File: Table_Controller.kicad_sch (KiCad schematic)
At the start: 173 parts, among them J10 1050171001 Micro Type B, J11 HX JN1.27-2x5 WZ H4.9, J12 Conn_01x04_Pin, J13 Conn_01x14_Pin, J14 2.54 mm header, J15 2.54 mm header, U10 STM32G431K8Tx, U11 LMR380x0, U12 VNH7070, Y10 20 MHz

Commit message: placement 95%
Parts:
- removed JP31: 0R, Resistor_THT:R_Axial_DIN0204_L3.6mm_D1.6mm_P5.08mm_Horizontal, symbol Device:R
- removed JP35: 0R, Personal:Jumper_0603, symbol Device:R
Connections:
- net S19V5: now also C25.1, C27.1, U12.12 (VCC), U12.4 (VCC), U12.5 (VCC)
- net S3V3: now also J14.4 (Pin_4)

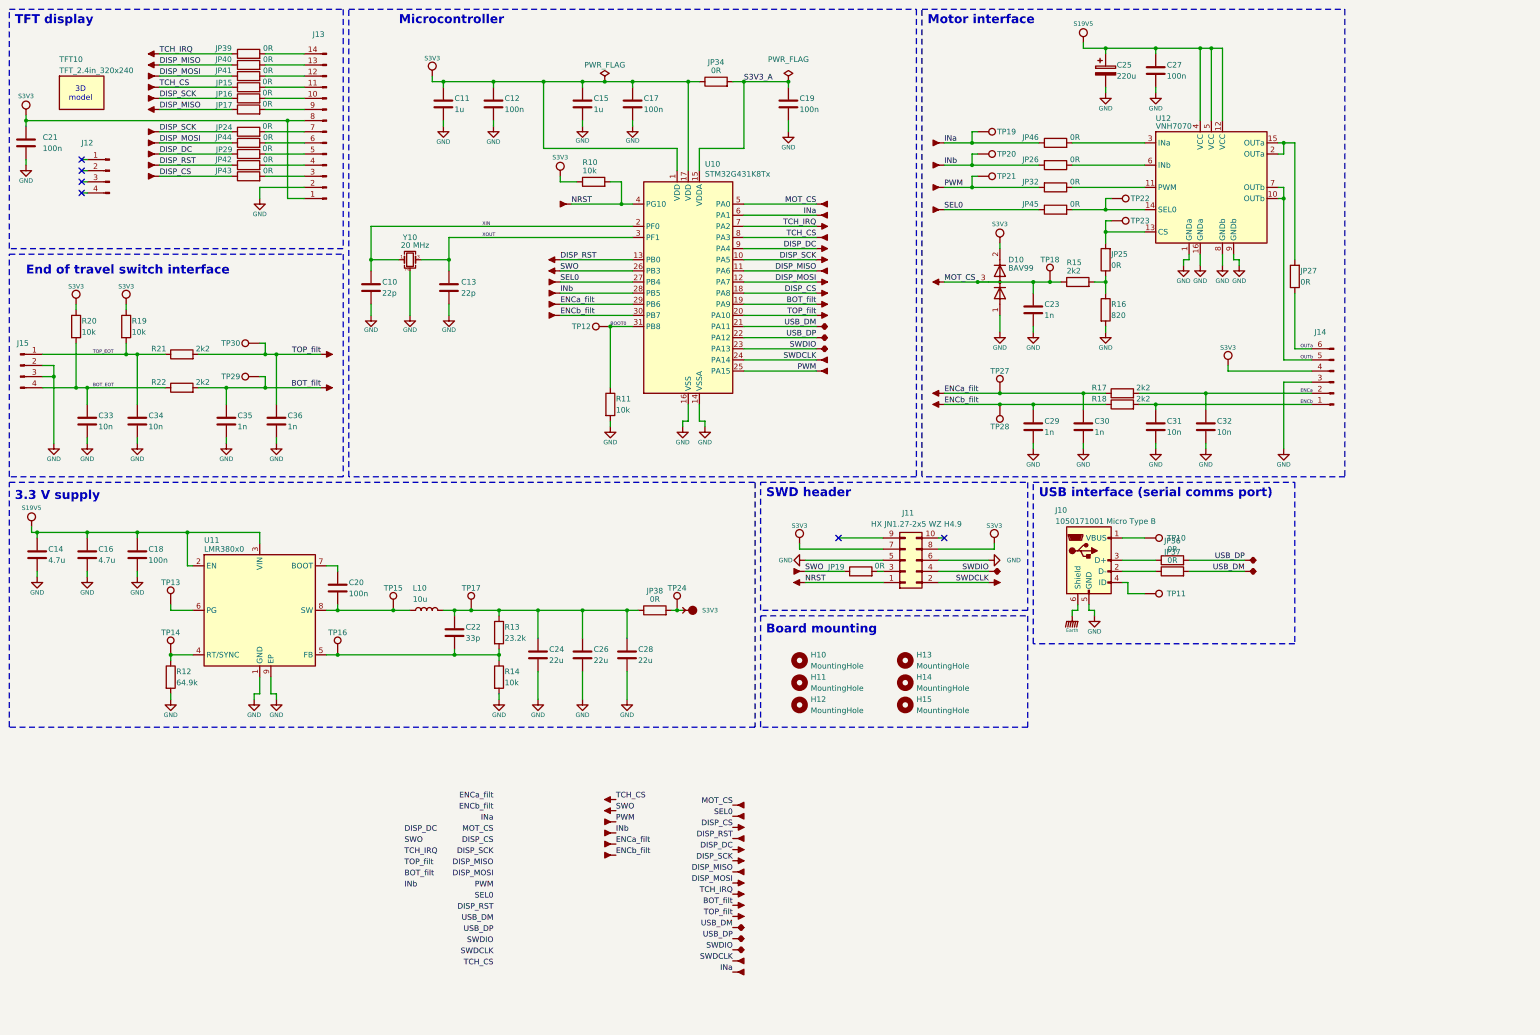
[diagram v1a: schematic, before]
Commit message: new usb connector
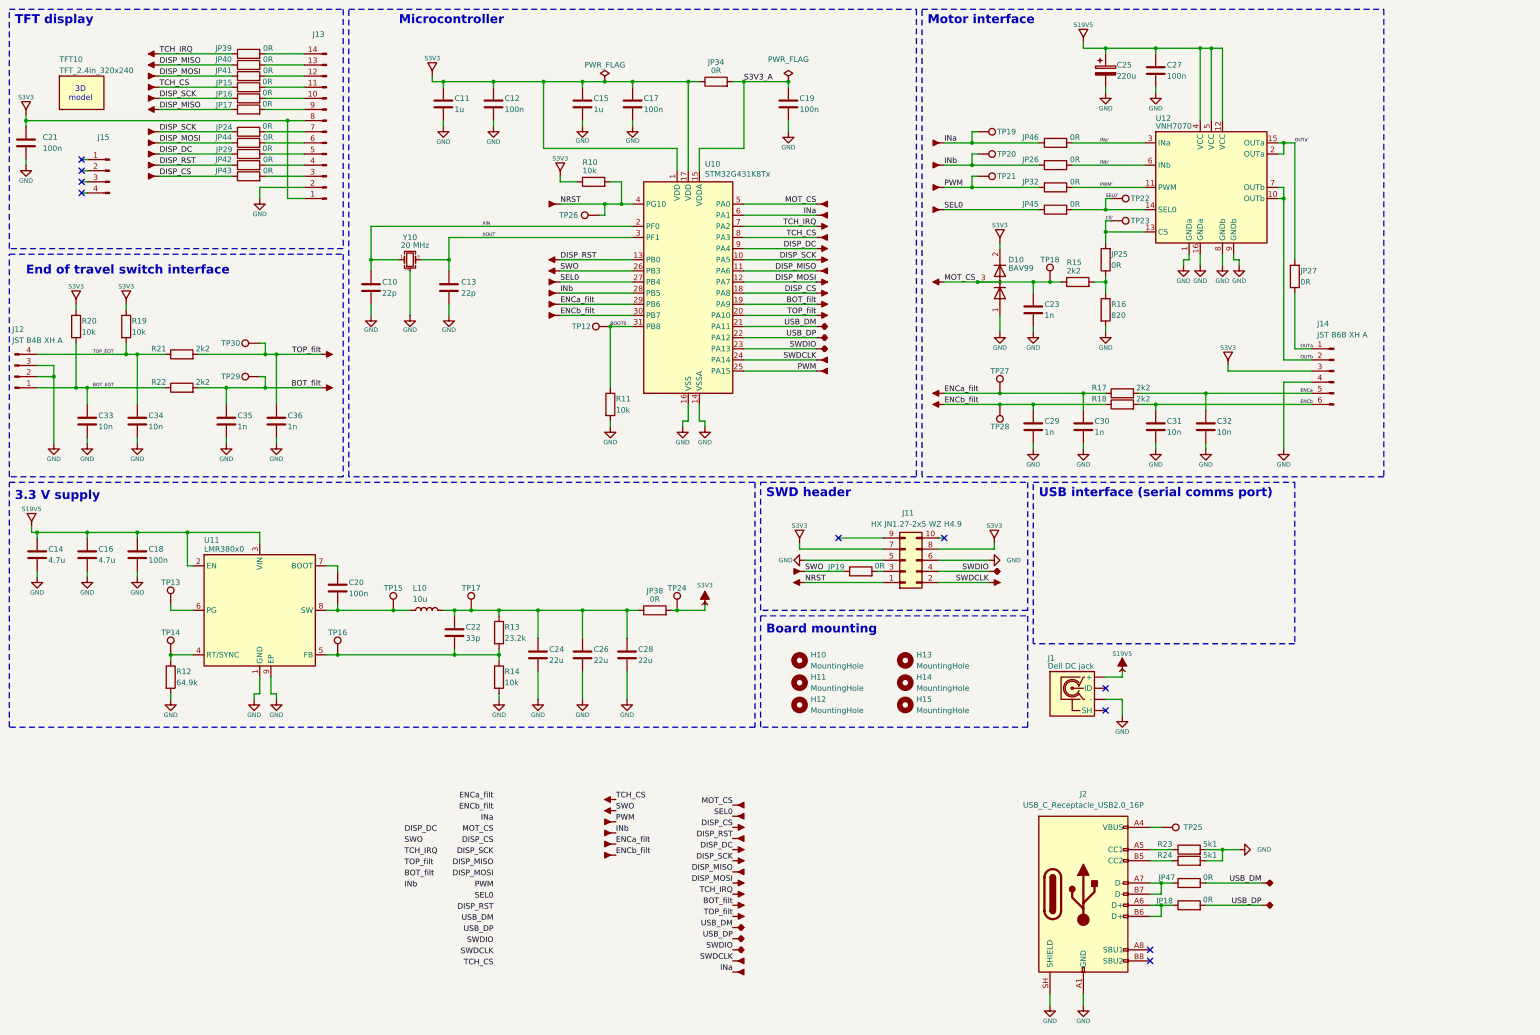
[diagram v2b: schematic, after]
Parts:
- removed J10: 1050171001 Micro Type B, Personal:USB_Micro-B_Molex-105017-0001, symbol Connector:USB_B_Micro
- removed JP36, JP37: 0R, Personal:Jumper_0603, symbol Device:R
- removed P14, P15: (no value), symbol personal:Cosmetic_IO
- removed TP10, TP11: TestPoint, TestPoint:TestPoint_THTPad_D1.0mm_Drill0.5mm, symbol Connector:TestPoint
- added J1: Dell DC jack, Personal:Dell DC jack, symbol personal:Dell_DC_barrel_jack
- added J2: USB_C_Receptacle_USB2.0_16P, Personal:USB_C_socket_16P_vertical, symbol Connector:USB_C_Receptacle_USB2.0_16P
- added JP18: 0R, Resistor_SMD:R_0603_1608Metric_Pad0.98x0.95mm_HandSolder, symbol Device:R
- added JP47: 0R, Personal:Jumper_0603, symbol Device:R
- added P81, P82: (no value), symbol personal:Cosmetic_IO
- added R23, R24: 5k1, Resistor_SMD:R_0603_1608Metric_Pad0.98x0.95mm_HandSolder, symbol Device:R
- added TP25, TP26: TestPoint, TestPoint:TestPoint_THTPad_D1.0mm_Drill0.5mm, symbol Connector:TestPoint
- J11: footprint Personal:HX JN1.27-2x5P ZZ H4.9 -> Personal:JN1.27-2x5 WZ H4.9
- J12: value Conn_01x04_Pin -> JST B4B XH A; footprint Connector_PinSocket_2.54mm:PinSocket_1x04_P2.54mm_Vertical -> Connector_JST:JST_XH_B4B-XH-A_1x04_P2.50mm_Vertical
- J14: value 2.54 mm header -> JST B6B XH A; footprint Connector_PinHeader_2.54mm:PinHeader_1x06_P2.54mm_Vertical -> Connector_JST:JST_XH_B6B-XH-A_1x06_P2.50mm_Vertical
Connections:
- net BOT_EOT: now also J12.1 (Pin_1); no longer J15.4 (Pin_4)
- net ENCa: now also J14.5 (Pin_5); no longer J14.2 (Pin_2)
- net ENCb: now also J14.6 (Pin_6); no longer J14.1 (Pin_1)
- net GND: now also J12.2 (Pin_2), J12.3 (Pin_3), J14.4 (Pin_4), J1.3 (-), J2.A1 (GND), J2.A12 (GND), J2.B1 (GND), J2.B12 (GND), J2.SH (SHIELD), R23.2, R24.2; no longer J14.3 (Pin_3), J15.2 (Pin_2), J15.3 (Pin_3)
- net NRST: now also TP26.1
- net OUTa: now also J14.1 (Pin_1); no longer J14.6 (Pin_6)
- net OUTb: now also J14.2 (Pin_2); no longer J14.5 (Pin_5)
- net S19V5: now also J1.1 (+)
- net S3V3: now also J14.3 (Pin_3); no longer J14.4 (Pin_4)
- net TOP_EOT: now also J12.4 (Pin_4); no longer J15.1 (Pin_1)
- net USB_DM: now also JP47.2, P82.1
- net USB_DP: now also JP18.2, P81.1
- net SEL0': now reaches JP45.2, TP22.1, U12.14 (SEL0)
- net CS': now reaches JP25.2, TP23.1, U12.13 (CS)
- net INa': now reaches JP46.2, U12.3 (INa)
- net PWM': now reaches JP32.1, U12.11 (PWM)
- net OUTa': now reaches JP27.2, U12.15 (OUTa), U12.2 (OUTa)
- net INb': now reaches JP26.1, U12.6 (INb)
- new net: J2.A5 (CC1), R23.1
- new net: J2.A4 (VBUS), J2.A9 (VBUS), J2.B4 (VBUS), J2.B9 (VBUS), TP25.1
- new net: J2.A6 (D+), J2.B6 (D+), JP18.1
- new net: J2.A7 (D-), J2.B7 (D-), JP47.1
- new net: J2.B5 (CC2), R24.1
- no-connect marks 6 -> 10
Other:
- moved on the sheet: J12, J14, J15

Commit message: concept placement finalised
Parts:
- removed JP15, JP16, JP24: 0R, Resistor_THT:R_Axial_DIN0204_L3.6mm_D1.6mm_P5.08mm_Horizontal, symbol Device:R
- removed JP26, JP32: 0R, Resistor_THT:R_Axial_DIN0204_L3.6mm_D1.6mm_P7.62mm_Horizontal, symbol Device:R
- removed TP19, TP20, TP21: TestPoint, TestPoint:TestPoint_THTPad_D1.0mm_Drill0.5mm, symbol Connector:TestPoint
- added JP20, JP21, JP22: 0R, Resistor_SMD:R_1206_3216Metric_Pad1.30x1.75mm_HandSolder, symbol Device:R
- added JP48, JP49: 0R, Personal:Jumper_0603, symbol Device:R
- added U1: USBLC6-2SC6, Package_TO_SOT_SMD:SOT-23-6, symbol Power_Protection:USBLC6-2SC6
- JP19: footprint Resistor_THT:R_Axial_DIN0204_L3.6mm_D1.6mm_P5.08mm_Horizontal -> Resistor_SMD:R_1206_3216Metric_Pad1.30x1.75mm_HandSolder
- JP25: footprint Resistor_THT:R_Axial_DIN0204_L3.6mm_D1.6mm_P7.62mm_Horizontal -> Resistor_SMD:R_1206_3216Metric_Pad1.30x1.75mm_HandSolder
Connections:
- net DISP_SCK: now also JP21.1, JP22.1
- net GND: now also U1.2 (GND)
- net INa: now also P19.1, U10.28 (PB5); no longer P24.1, U10.6 (PA1)
- net INb: now also P18.1, U10.27 (PB4), JP48.1; no longer P19.1, U10.28 (PB5)
- net INb': now also JP48.2
- net OUTa: now also J14.2 (Pin_2), U12.15 (OUTa), U12.2 (OUTa); no longer J14.1 (Pin_1), JP27.1
- net OUTa': no longer JP27.2, U12.15 (OUTa), U12.2 (OUTa)
- net OUTb: now also J14.1 (Pin_1), JP27.1; no longer J14.2 (Pin_2), U12.10 (OUTb), U12.7 (OUTb)
- net PWM: now also JP49.1
- net PWM': now also JP49.2
- net S3V3: now also U1.5 (VBUS)
- net SEL0: now also P24.1, TP22.1, U10.6 (PA1); no longer P18.1, U10.27 (PB4)
- net SEL0': no longer TP22.1
- net TCH_CS: now also JP20.1
- net USB_DM: now also U1.1 (I/O1); no longer JP47.2
- net USB_DP: now also U1.3 (I/O2); no longer JP18.2
- net at J13.11 (Pin_11): now also JP20.2
- net at J13.10 (Pin_10): now also JP21.2
- net at J13.7 (Pin_7): now also JP22.2
- new net: JP18.2, U1.4 (I/O2)
- new net: JP47.2, U1.6 (I/O1)
- new net: JP27.2, U12.10 (OUTb), U12.7 (OUTb)
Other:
- moved on the sheet: JP18, JP47, R23, R24, TP22

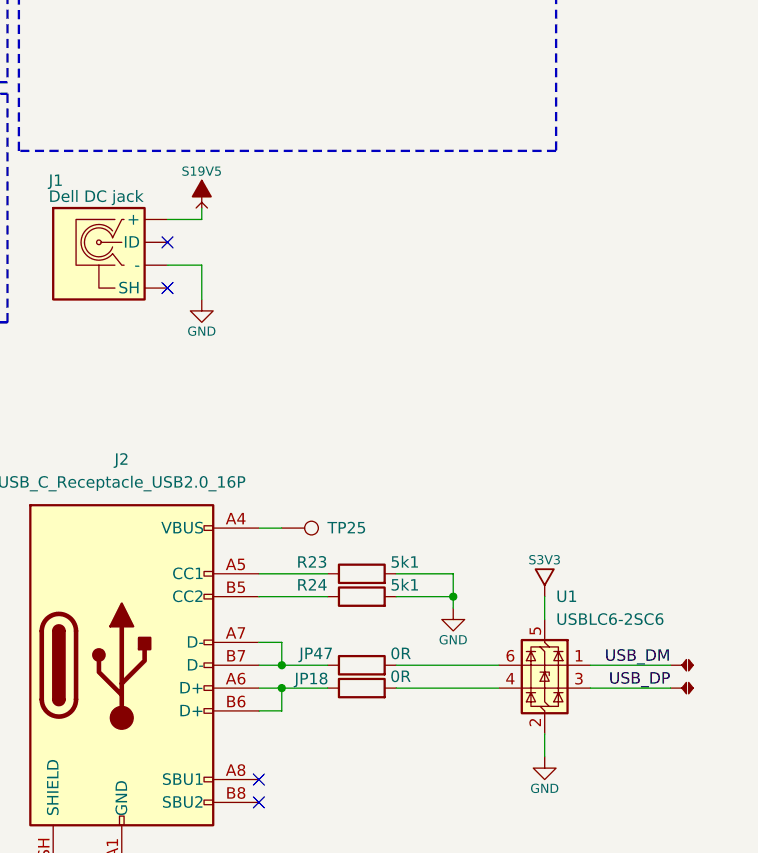
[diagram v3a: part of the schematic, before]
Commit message: reworked DC barrel jack
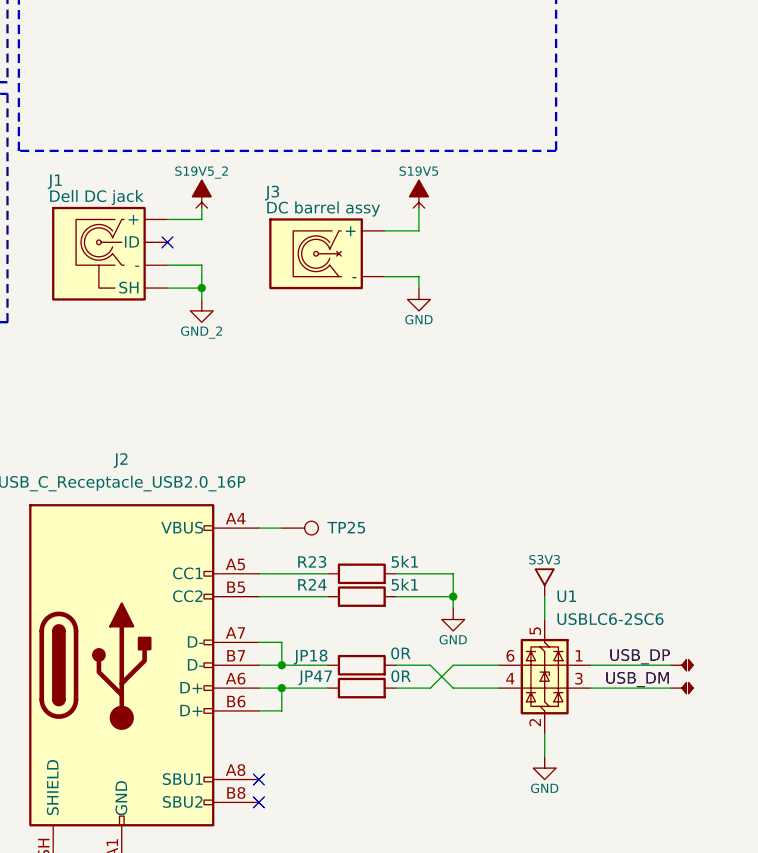
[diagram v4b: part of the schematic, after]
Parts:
- added J3: DC barrel assy, Personal:Dell_barrel_assy, symbol personal:DC_barrel_assy
- TFT10: footprint Personal:Display_240x320_ILI9341_2.4in -> Personal:Display_240x320_ILI9341_2.4in_no_pads
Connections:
- net GND: now also J3.3 (-); no longer J1.3 (-)
- net S19V5: now also J3.1 (+); no longer J1.1 (+)
- net USB_DM: now also U1.3 (I/O2); no longer U1.1 (I/O1)
- net USB_DP: now also U1.1 (I/O1); no longer U1.3 (I/O2)
- net at J2.A6 (D+), J2.B6 (D+): now also JP47.1; no longer JP18.1
- net at J2.A7 (D-), J2.B7 (D-): now also JP18.1; no longer JP47.1
- net GND_2: now reaches J1.SH
- net GND_2: now also J1.3 (-)
- new net S19V5_2: J1.1 (+)
- no-connect marks 10 -> 9
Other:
- moved on the sheet: JP18, JP47

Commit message: sch erc done, clear
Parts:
- removed P55, P56, P60, P65, P73, P74, P77, P78, P79, P80: (no value), symbol personal:Cosmetic_IN
- removed P59, P63, P64, P66, P67, P68, P69, P75, P76: (no value), symbol personal:Cosmetic_OUT
- removed P70, P71, P72: (no value), symbol personal:Cosmetic_IO
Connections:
- net CC1: now reaches J2.A5 (CC1), R23.1
- net 3V3_REG: now reaches C22.1, C24.1, C26.1, C28.1, JP38.1, L10.2, R13.1, TP17.1
- net D+: now reaches J2.A6 (D+), J2.B6 (D+), JP47.1
- net D-: now reaches J2.A7 (D-), J2.B7 (D-), JP18.1
- net CC2: now reaches J2.B5 (CC2), R24.1
- net RT: now reaches R12.1, TP14.1, U11.4 (RT/SYNC)
- net D-': now reaches JP18.2, U1.4 (I/O2)
- net D+': now reaches JP47.2, U1.6 (I/O1)
- net FB: now reaches C22.2, R13.2, R14.1, TP16.1, U11.5 (FB)
- net SW: now reaches C20.2, L10.1, TP15.1, U11.8 (SW)
- net PG: now reaches TP13.1, U11.6 (PG)
- net SWO': now reaches J11.3 (Pin_3), JP19.2
- net OUTb': now reaches JP27.2, U12.10 (OUTb), U12.7 (OUTb)
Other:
- company: ${COMPANY} -> CC
- moved on the sheet: C10, C13, J1, J11, J3, JP18, JP47, R23, R24, Y10

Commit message: routing 50%
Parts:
- removed H10, H11, H12, H13, H14, H15: MountingHole, MountingHole:MountingHole_3.2mm_M3, symbol Mechanical:MountingHole
- removed JP45: 0R, Personal:Jumper_0603, symbol Device:R
- added JP28: 0R, Resistor_THT:R_Axial_DIN0204_L3.6mm_D1.6mm_P7.62mm_Horizontal, symbol Device:R
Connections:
- net SEL0: now also JP28.2
- net SEL0': now also JP28.1
